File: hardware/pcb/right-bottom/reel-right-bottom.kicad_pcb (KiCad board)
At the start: 2 copper layers, 134.6 x 86.9 mm, 47 parts, among them J1 Conn_01x02, J3 Conn_01x05, SW1 SW_Push, SW10 SW_Push, SW11 SW_Push, SW12 SW_Push, SW13 SW_Push, SW14 SW_Push, SW15 SW_Push, SW16 SW_Push, SW17 SW_Push, SW18 SW_Push, SW19 SW_Push, SW2 SW_Push, SW22 SW_SPDT, SW3 SW_Push, SW4 SW_Push, SW5 SW_Push, SW6 SW_Push, SW7 SW_Push, SW8 SW_Push, SW9 SW_Push

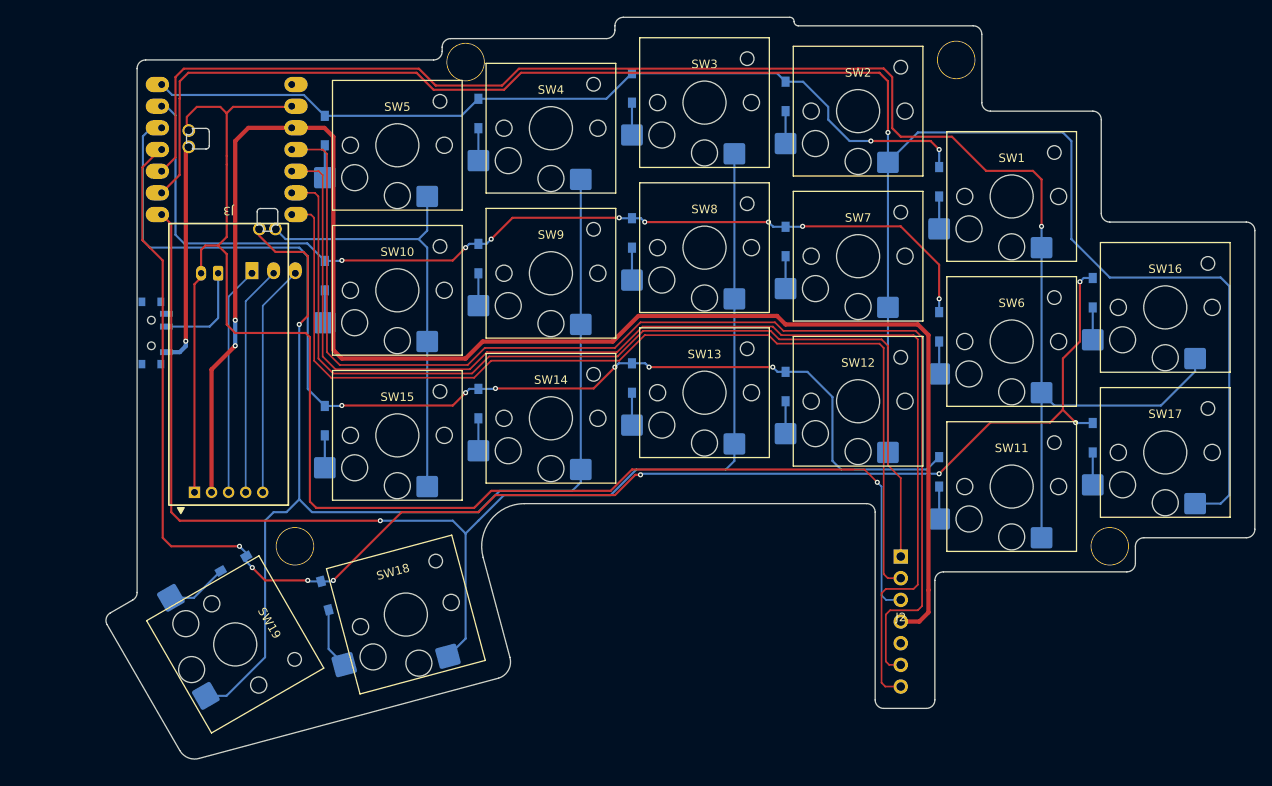
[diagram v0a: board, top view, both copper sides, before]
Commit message: Add right-bottom plate PCB and STEP model
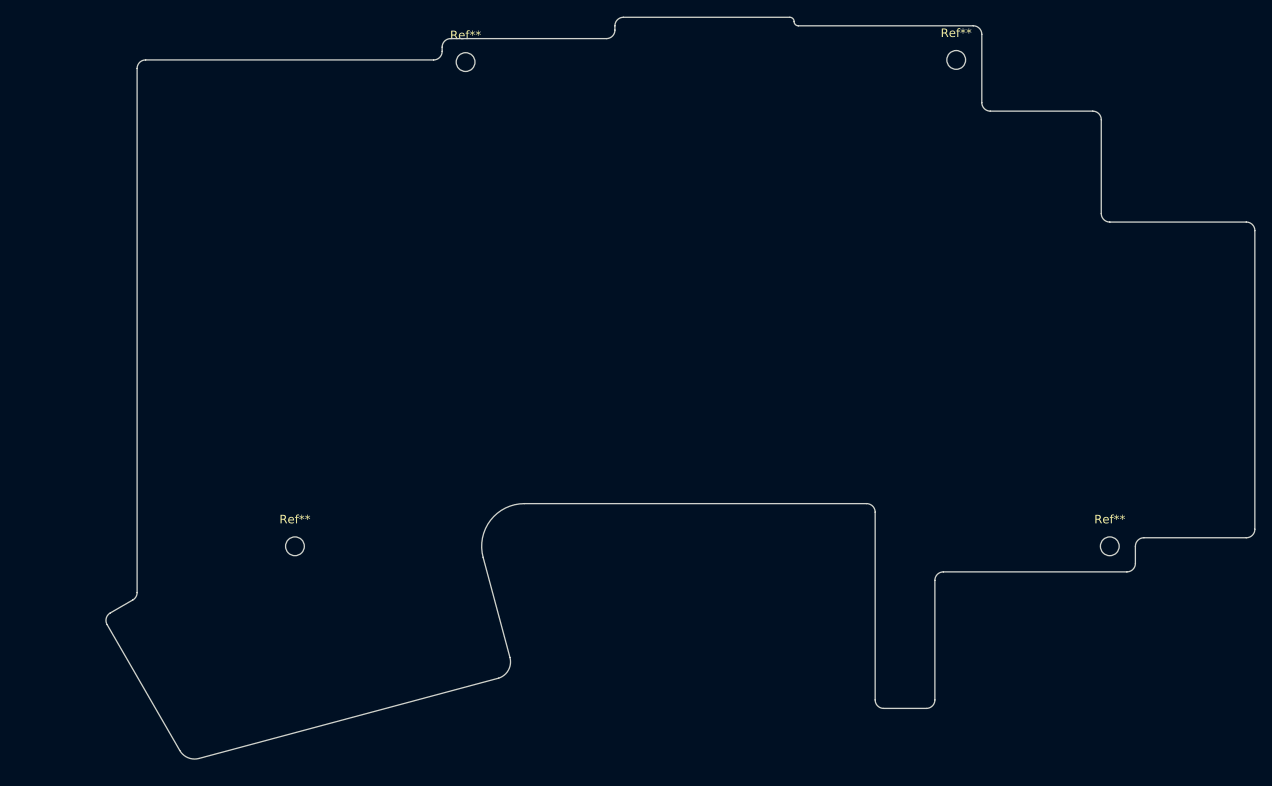
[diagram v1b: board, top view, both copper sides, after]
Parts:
- removed D1, D10, D11, D12, D13, D14, D15, D16, D17, D18, D19, D2, D3, D4, D5, D6, D7, D8, D9: D, reel:Diode_SMD
- removed J1: Conn_01x02, Connector_JST:JST_PH_S2B-PH-K_1x02_P2.00mm_Horizontal
- removed J2: ~, reel:pmw3610_connector
- removed J3: Conn_01x05, reel:Display_BeeKeeb_MIP_1.08in_LS011B7DH03
- removed SW1, SW10, SW11, SW12, SW13, SW14, SW15, SW16, SW17, SW18, SW19, SW2, SW3, SW4, SW5, SW6, SW7, SW8, SW9: SW_Push, reel:SW_Hotswap_Kailh_Choc_V1V2_1.00u
- removed SW22: SW_SPDT, Button_Switch_SMD:SW_SPDT_PCM12
- removed U1: ~, reel:XIAO_nRF52840_wBAT_wNFC_1
- Ref** (x4): footprint reel:m2_Spacer_Hole -> MountingHole:MountingHole_2.2mm_M2
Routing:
- net Col1: track 227.5 -> 0.00 mm, vias 1 -> 0
- net 3.3V: track 189.3 -> 0.00 mm, vias 2 -> 0
- net Col0: track 187.9 -> 0.00 mm, vias 1 -> 0
- net GND: track 186.2 -> 0.00 mm, vias 1 -> 0
- net Row3: track 185.8 -> 0.00 mm, vias 8 -> 0
- net Col2: track 157.1 -> 0.00 mm, vias 1 -> 0
- net MOTION: track 144.5 -> 0.00 mm
- net SDIO: track 144.3 -> 0.00 mm
- net Row2: track 137.5 -> 0.00 mm, vias 6 -> 0
- net Col3: track 136.1 -> 0.00 mm, vias 1 -> 0
- net nCS: track 118.5 -> 0.00 mm
- net SCLK: track 117.5 -> 0.00 mm
- net Row1: track 116.8 -> 0.00 mm, vias 8 -> 0
- net Row0: track 101.4 -> 0.00 mm, vias 2 -> 0
- net Col4: track 51.8 -> 0.00 mm
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
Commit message: Update ReeL hardware and fabrication assets
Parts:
- added Ref**: Val**, MountingHole:MountingHole_2.2mm_M2, F.Cu at (137.5, 107.5)
- moved Ref** 10.0 mm to (58.0, 107.5)
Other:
- board size 134.6 x 86.9 mm -> 143 x 86.6 mm
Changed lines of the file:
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@@
+	(footprint "MountingHole:MountingHole_2.2mm_M2"
+		(layer "F.Cu")
+		(at 137.5 107.5)
+		(descr "Mounting Hole 2.2mm, M2, no annular, generated by kicad-footprint-generator mountinghole.py")
+		(tags "mountinghole M2")
+		(property "Reference" "Ref**"
+			(at 0 -3.15 0)
+			(layer "F.SilkS")
+			(effects
+				(font
+					(size 1 1)
+					(thickness 0.15)
+				)
+			)
+		)
+		(property "Value" "Val**"
+			(at 0 3.15 0)
+			(layer "F.Fab")
+			(effects
+				(font
+					(size 1 1)
+					(thickness 0.15)
+				)
+			)
+		)
+		(property "Datasheet" ""
+			(at 0 0 0)
+			(layer "F.Fab")
+			(hide yes)
+			(effects
+				(font
+					(size 1.27 1.27)
+				)
+			)
+		)
+		(property "Description" ""
+			(at 0 0 0)
+			(layer "F.Fab")
+			(hide yes)
+			(effects
+				(font
+					(size 1.27 1.27)
+				)
+			)
+		)
+		(property "KiLib_Generator" "mounting_hardware/mounting_hole"
+			(at 0 0 0)
+			(layer "F.SilkS")
+			(hide yes)
+			(effects
+				(font
+					(size 1 1)
+					(thickness 0.15)
+				)
+			)
+		)
+		(attr exclude_from_pos_files exclude_from_bom)
+		(duplicate_pad_numbers_are_jumpers no)
+		(fp_circle
+			(center 0 0)
+			(end 2.2 0)
+			(stroke
+				(width 0.15)
+				(type solid)
+			)
+			(fill no)
+			(layer "Cmts.User")
+		)
+		(fp_circle
+			(center 0 0)
+			(end 2.45 0)
+			(stroke
+				(width 0.05)
+				(type solid)
+			)
+			(fill no)
+			(layer "F.CrtYd")
+		)
+		(fp_text user "${REFERENCE}"
+			(at 0 0 0)
+			(layer "F.Fab")
+			(effects
+				(font
+					(size 1 1)
+					(thickness 0.15)
+				)
+			)
+		)
+		(pad "" np_thru_hole circle
+			(at 0 0)
+			(size 2.2 2.2)
+			(drill 2.2)
+			(layers "*.Cu" "*.Mask")
+		)
+		(embedded_fonts no)
+	)
 	(footprint "MountingHole:MountingHole_2.2mm_M2"
 		(layer "F.Cu")
@@
 	(footprint "MountingHole:MountingHole_2.2mm_M2"
 		(layer "F.Cu")
-		(at 68 107.5)
+		(at 58 107.5)
 		(descr "Mounting Hole 2.2mm, M2, no annular, generated by kicad-footprint-generator mountinghole.py")
 		(tags "mountinghole M2")
@@
 	)
 	(gr_arc
-		(start 45.986856 116.683017)
-		(mid 45.886954 115.924197)
-		(end 46.35288 115.31699)
-		(stroke
-			(width 0.05)
-			(type default)
-		)
-		(layer "Edge.Cuts")
-	)
-	(gr_line
-		(start 45.986856 116.683017)
-		(end 54.503472 131.434154)
+		(start 37.589746 115.772758)
+		(mid 37.489877 115.013958)
+		(end 37.955771 114.406733)
+		(stroke
+			(width 0.05)
+			(type default)
+		)
+		(layer "Edge.Cuts")
+	)
+	(gr_line
+		(start 37.589746 115.772758)
+		(end 46.722209 131.590648)
 		(stroke
 			(width 0.05)
@@
 	)
 	(gr_line
-		(start 46.35288 115.31699)
-		(end 49 113.788675)
+		(start 37.955771 114.406733)
+		(end 47 109.185045)
 		(stroke
 			(width 0.05)
@@
 		(layer "Edge.Cuts")
 	)
+	(gr_arc
+		(start 47.847054 132.056574)
+		(mid 47.205532 132.014546)
+		(end 46.722209 131.590648)
+		(stroke
+			(width 0.05)
+			(type default)
+		)
+		(layer "Edge.Cuts")
+	)
 	(gr_line
 		(start 49.5 51.5)
-		(end 49.5 112.92265)
+		(end 49.5 104.854918)
 		(stroke
 			(width 0.05)
@@
 	)
 	(gr_arc
-		(start 49.5 112.92265)
-		(mid 49.366025 113.42265)
-		(end 49 113.788675)
+		(start 49.5 104.854918)
+		(mid 48.83012 107.354912)
+		(end 47 109.185045)
 		(stroke
 			(width 0.05)
@@
 	)
 	(gr_arc
-		(start 56.753158 132.366002)
-		(mid 55.470155 132.28191)
-		(end 54.503472 131.434154)
+		(start 80.609457 110.794095)
+		(mid 81.47232 106.456193)
+		(end 85.439086 104.5)
+		(stroke
+			(width 0.05)
+			(type default)
+		)
+		(layer "Edge.Cuts")
+	)
+	(gr_line
+		(start 82.764485 122.700476)
+		(end 47.847054 132.056574)
+		(stroke
+			(width 0.05)
+			(type solid)
+		)
+		(layer "Edge.Cuts")
+	)
+	(gr_line
+		(start 83.471592 121.475731)
+		(end 80.609457 110.794095)
+		(stroke
+			(width 0.05)
+			(type solid)
+		)
+		(layer "Edge.Cuts")
+	)
+	(gr_arc
+		(start 83.471592 121.475731)
+		(mid 83.371665 122.234514)
+		(end 82.764485 122.700476)
 		(stroke
 			(width 0.05)
@@
 	)
 	(gr_line
-		(start 90.052523 108.794095)
-		(end 93.19777 120.532314)
+		(start 89.5 104.5)
+		(end 85.439086 104.5)
+		(stroke
+			(width 0.05)
+			(type default)
+		)
+		(layer "Edge.Cuts")
+	)
+	(gr_arc
+		(start 90.5 103.5)
+		(mid 90.207107 104.207107)
+		(end 89.5 104.5)
+		(stroke
+			(width 0.05)
+			(type default)
+		)
+		(layer "Edge.Cuts")
+	)
+	(gr_arc
+		(start 90.5 103.5)
+		(mid 90.792893 102.792893)
+		(end 91.5 102.5)
+		(stroke
+			(width 0.05)
+			(type default)
+		)
+		(layer "Edge.Cuts")
+	)
+	(gr_line
+		(start 91.5 102.5)
+		(end 125 102.5)
 		(stroke
 			(width 0.05)
 			(type solid)
-		)
-		(layer "Edge.Cuts")
-	)
-	(gr_arc
-		(start 90.052523 108.794095)
-		(mid 90.915386 104.456193)
-		(end 94.882152 102.5)
-		(stroke
-			(width 0.05)
-			(type default)
-		)
-		(layer "Edge.Cuts")
-	)
-	(gr_line
-		(start 91.871403 122.956097)
-		(end 56.753158 132.366002)
-		(stroke
-			(width 0.05)
-			(type solid)
-		)
-		(layer "Edge.Cuts")
-	)
-	(gr_arc
-		(start 93.19777 120.532314)
-		(mid 93.020424 122.010086)
-		(end 91.871403 122.956097)
-		(stroke
-			(width 0.05)
-			(type default)
 		)
 		(layer "Edge.Cuts")
@@
 	)
 	(gr_arc
+		(start 125 102.5)
+		(mid 125.707107 102.792893)
+		(end 126 103.5)
+		(stroke
+			(width 0.05)
+			(type default)
+		)
+		(layer "Edge.Cuts")
+	)
+	(gr_arc
 		(start 126 45.5)
 		(mid 126.353553 45.646447)
@@
 		(layer "Edge.Cuts")
 	)
+	(gr_line
+		(start 126 126)
+		(end 126 103.5)
+		(stroke
+			(width 0.05)
+			(type solid)
+		)
+		(layer "Edge.Cuts")
+	)
 	(gr_arc
 		(start 127 46.5)
@@
 		(layer "Edge.Cuts")
 	)
-	(gr_line
-		(start 135 102.5)
-		(end 94.882152 102.5)
-		(stroke
-			(width 0.05)
-			(type default)
-		)
-		(layer "Edge.Cuts")
-	)
-	(gr_arc
-		(start 135 102.5)
-		(mid 135.707107 102.792893)
-		(end 136 103.5)
-		(stroke
-			(width 0.05)
-			(type default)
-		)
-		(layer "Edge.Cuts")
-	)
-	(gr_line
-		(start 136 125.5)
-		(end 136 103.5)
+	(gr_arc
+		(start 127 127)
+		(mid 126.292893 126.707107)
+		(end 126 126)
+		(stroke
+			(width 0.05)
+			(type default)
+		)
+		(layer "Edge.Cuts")
+	)
+	(gr_line
+		(start 132 127)
+		(end 127 127)
 		(stroke
 			(width 0.05)
@@
 		(layer "Edge.Cuts")
 	)
-	(gr_arc
-		(start 137 126.5)
-		(mid 136.292893 126.207107)
-		(end 136 125.5)
-		(stroke
-			(width 0.05)
-			(type default)
-		)
-		(layer "Edge.Cuts")
-	)
-	(gr_line
-		(start 142 126.5)
-		(end 137 126.5)
-		(stroke
-			(width 0.05)
-			(type default)
-		)
-		(layer "Edge.Cuts")
-	)
-	(gr_line
-		(start 143 111.5)
-		(end 143 125.5)
-		(stroke
-			(width 0.05)
-			(type default)
-		)
-		(layer "Edge.Cuts")
-	)
-	(gr_arc
-		(start 143 111.5)
-		(mid 143.292893 110.792893)
-		(end 144 110.5)
-		(stroke
-			(width 0.05)
-			(type default)
-		)
-		(layer "Edge.Cuts")
-	)
-	(gr_arc
-		(start 143 125.5)
-		(mid 142.707107 126.207107)
-		(end 142 126.5)
+	(gr_line
+		(start 133 110.5)
+		(end 133 126)
+		(stroke
+			(width 0.05)
+			(type solid)
+		)
+		(layer "Edge.Cuts")
+	)
+	(gr_arc
+		(start 133 126)
+		(mid 132.707107 126.707107)
+		(end 132 127)
 		(stroke
 			(width 0.05)
@@
 	(gr_line
 		(start 165.5 110.5)
-		(end 144 110.5)
-		(stroke
-			(width 0.05)
+		(end 133 110.5)
+		(stroke
+			(width 0.05)

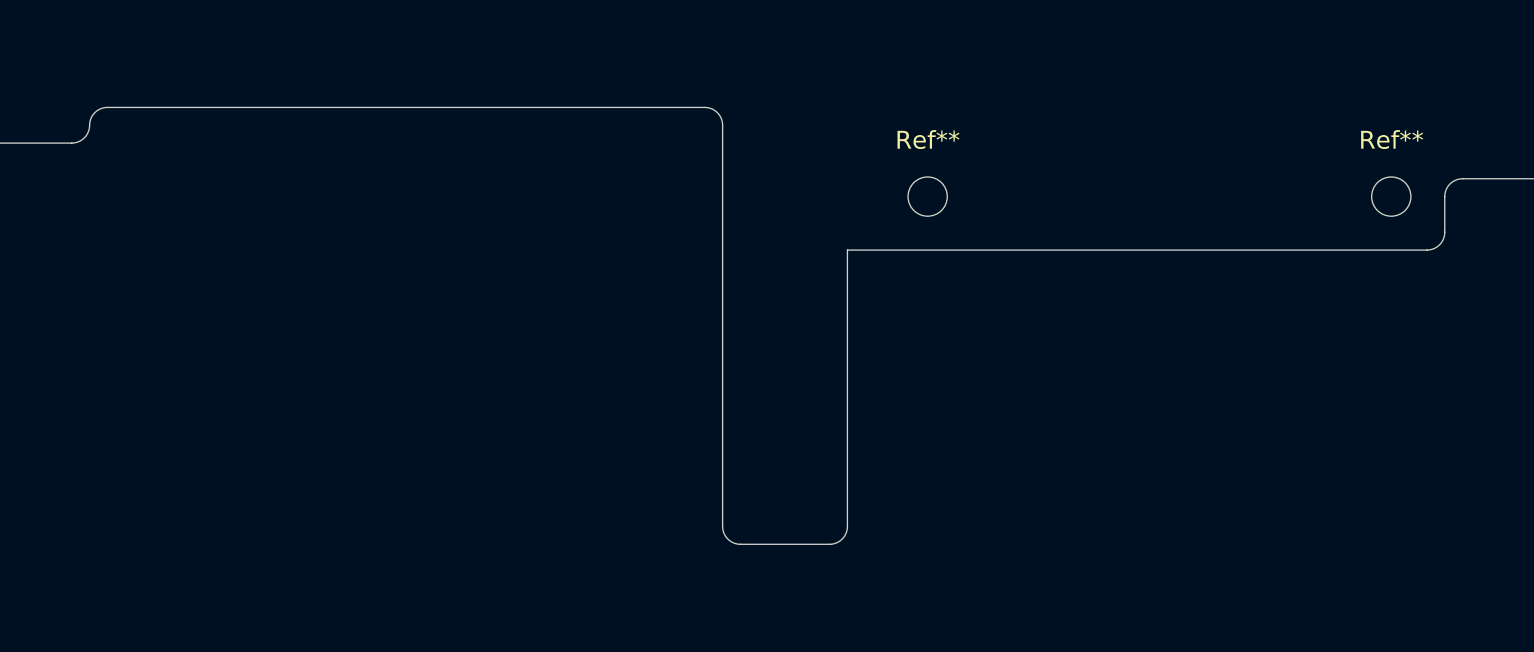
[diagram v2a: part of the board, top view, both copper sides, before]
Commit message: Update right plate PCB models
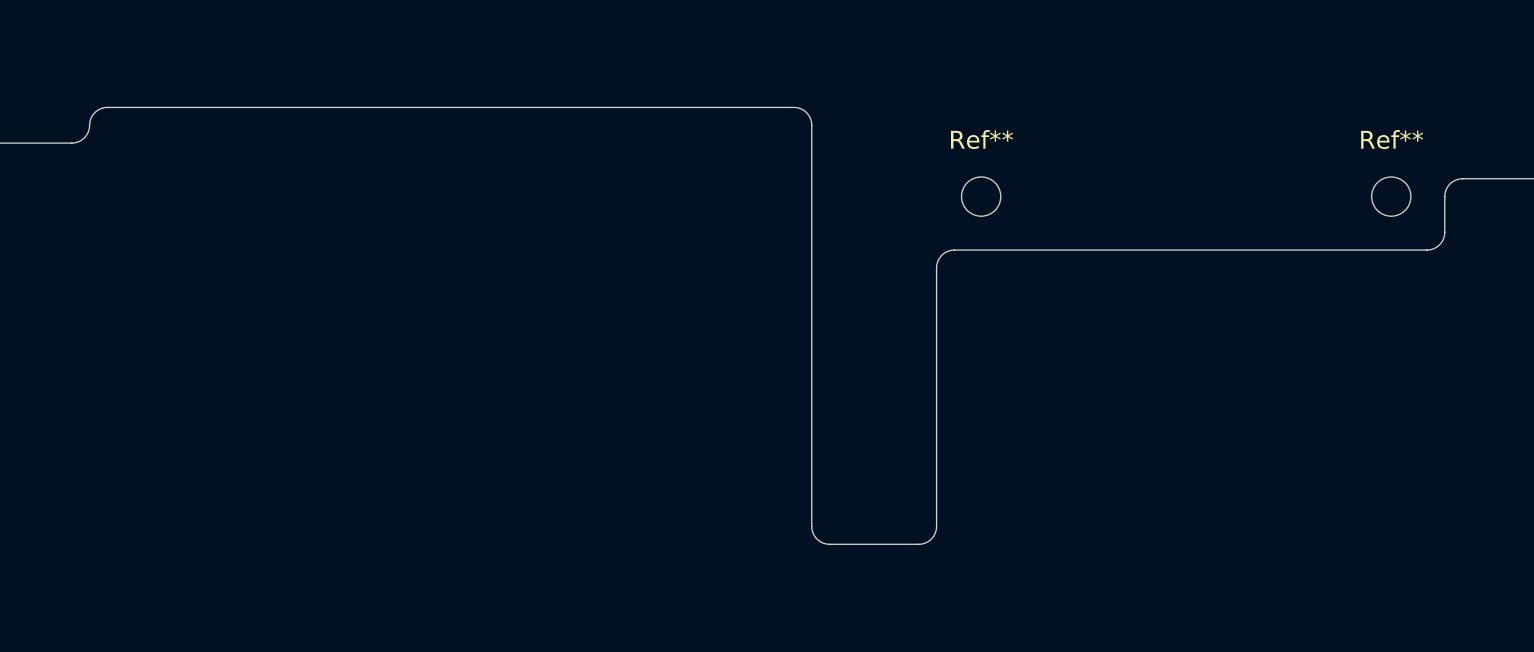
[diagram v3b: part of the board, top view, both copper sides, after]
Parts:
- Ref** (x5): value Val** -> MountingHole_2.2mm_M2
- moved Ref** 3.00 mm to (140.5, 107.5)
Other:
- outline, holes or cut-outs redrawn
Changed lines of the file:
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@@
 		(filling no)
 		(pcbplotparams
-			(layerselection 0x00000000_00000000_55555555_57555550)
+			(layerselection 0x00000000_00000000_55555555_5755f5ff)
 			(plot_on_all_layers_selection 0x00000000_00000000_00000000_00000000)
 			(disableapertmacros no)
@@
 			(crossoutdnponfab yes)
 			(subtractmaskfromsilk no)
-			(outputformat 3)
+			(outputformat 1)
 			(mirror no)
 			(drillshape 0)
@@
 	(footprint "MountingHole:MountingHole_2.2mm_M2"
 		(layer "F.Cu")
-		(at 137.5 107.5)
+		(at 140.5 107.5)
 		(descr "Mounting Hole 2.2mm, M2, no annular, generated by kicad-footprint-generator mountinghole.py")
 		(tags "mountinghole M2")
@@
 			)
 		)
-		(property "Value" "Val**"
+		(property "Value" "MountingHole_2.2mm_M2"
 			(at 0 3.15 0)
 			(layer "F.Fab")
@@
 					(size 1 1)
 					(thickness 0.15)
-				)
-			)
-		)
-		(property "Datasheet" ""
-			(at 0 0 0)
-			(layer "F.Fab")
-			(hide yes)
-			(effects
-				(font
-					(size 1.27 1.27)
-				)
-			)
-		)
-		(property "Description" ""
-			(at 0 0 0)
-			(layer "F.Fab")
-			(hide yes)
-			(effects
-				(font
-					(size 1.27 1.27)
 				)
 			)
@@
 			)
 		)
-		(property "Value" "Val**"
+		(property "Value" "MountingHole_2.2mm_M2"
 			(at 0 3.15 0)
 			(layer "F.Fab")
@@
 					(size 1 1)
 					(thickness 0.15)
-				)
-			)
-		)
-		(property "Datasheet" ""
-			(at 0 0 0)
-			(layer "F.Fab")
-			(hide yes)
-			(effects
-				(font
-					(size 1.27 1.27)
-				)
-			)
-		)
-		(property "Description" ""
-			(at 0 0 0)
-			(layer "F.Fab")
-			(hide yes)
-			(effects
-				(font
-					(size 1.27 1.27)
 				)
 			)
@@
 			)
 		)
-		(property "Value" "Val**"
+		(property "Value" "MountingHole_2.2mm_M2"
 			(at 0 3.15 0)
 			(layer "F.Fab")
@@
 					(size 1 1)
 					(thickness 0.15)
-				)
-			)
-		)
-		(property "Datasheet" ""
-			(at 0 0 0)
-			(layer "F.Fab")
-			(hide yes)
-			(effects
-				(font
-					(size 1.27 1.27)
-				)
-			)
-		)
-		(property "Description" ""
-			(at 0 0 0)
-			(layer "F.Fab")
-			(hide yes)
-			(effects
-				(font
-					(size 1.27 1.27)
 				)
 			)
@@
 			)
 		)
-		(property "Value" "Val**"
+		(property "Value" "MountingHole_2.2mm_M2"
 			(at 0 3.15 0)
 			(layer "F.Fab")
@@
 					(size 1 1)
 					(thickness 0.15)
-				)
-			)
-		)
-		(property "Datasheet" ""
-			(at 0 0 0)
-			(layer "F.Fab")
-			(hide yes)
-			(effects
-				(font
-					(size 1.27 1.27)
-				)
-			)
-		)
-		(property "Description" ""
-			(at 0 0 0)
-			(layer "F.Fab")
-			(hide yes)
-			(effects
-				(font
-					(size 1.27 1.27)
 				)
 			)
@@
 			)
 		)
-		(property "Value" "Val**"
+		(property "Value" "MountingHole_2.2mm_M2"
 			(at 0 3.15 0)
 			(layer "F.Fab")
@@
 					(size 1 1)
 					(thickness 0.15)
-				)
-			)
-		)
-		(property "Datasheet" ""
-			(at 0 0 0)
-			(layer "F.Fab")
-			(hide yes)
-			(effects
-				(font
-					(size 1.27 1.27)
-				)
-			)
-		)
-		(property "Description" ""
-			(at 0 0 0)
-			(layer "F.Fab")
-			(hide yes)
-			(effects
-				(font
-					(size 1.27 1.27)
 				)
 			)
@@
 	(gr_line
 		(start 91.5 102.5)
-		(end 125 102.5)
+		(end 130 102.5)
 		(stroke
 			(width 0.05)
@@
 	)
 	(gr_arc
-		(start 125 102.5)
-		(mid 125.707107 102.792893)
-		(end 126 103.5)
-		(stroke
-			(width 0.05)
-			(type default)
-		)
-		(layer "Edge.Cuts")
-	)
-	(gr_arc
 		(start 126 45.5)
 		(mid 126.353553 45.646447)
@@
 		(layer "Edge.Cuts")
 	)
-	(gr_line
-		(start 126 126)
-		(end 126 103.5)
-		(stroke
-			(width 0.05)
-			(type solid)
-		)
-		(layer "Edge.Cuts")
-	)
 	(gr_arc
 		(start 127 46.5)
@@
 	)
 	(gr_arc
-		(start 127 127)
-		(mid 126.292893 126.707107)
-		(end 126 126)
-		(stroke
-			(width 0.05)
-			(type default)
-		)
-		(layer "Edge.Cuts")
-	)
-	(gr_line
+		(start 130 102.5)
+		(mid 130.707107 102.792893)
+		(end 131 103.5)
+		(stroke
+			(width 0.05)
+			(type default)
+		)
+		(layer "Edge.Cuts")
+	)
+	(gr_line
+		(start 131 126)
+		(end 131 103.5)
+		(stroke
+			(width 0.05)
+			(type solid)
+		)
+		(layer "Edge.Cuts")
+	)
+	(gr_arc
 		(start 132 127)
-		(end 127 127)
+		(mid 131.292893 126.707107)
+		(end 131 126)
+		(stroke
+			(width 0.05)
+			(type default)
+		)
+		(layer "Edge.Cuts")
+	)
+	(gr_line
+		(start 137 127)
+		(end 132 127)
 		(stroke
 			(width 0.05)
@@
 	)
 	(gr_line
-		(start 133 110.5)
-		(end 133 126)
+		(start 138 111.5)
+		(end 138 126)
 		(stroke
 			(width 0.05)
@@
 	)
 	(gr_arc
-		(start 133 126)
-		(mid 132.707107 126.707107)
-		(end 132 127)
+		(start 138 111.5)
+		(mid 138.292893 110.792893)
+		(end 139 110.5)
+		(stroke
+			(width 0.05)
+			(type default)
+		)
+		(layer "Edge.Cuts")
+	)
+	(gr_arc
+		(start 138 126)
+		(mid 137.707107 126.707107)
+		(end 137 127)
 		(stroke
 			(width 0.05)
@@
 	(gr_line
 		(start 165.5 110.5)
-		(end 133 110.5)
-		(stroke
-			(width 0.05)
+		(end 139 110.5)
+		(stroke
+			(width 0.05)
